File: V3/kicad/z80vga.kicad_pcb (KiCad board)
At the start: 2 copper layers, 135 x 100 mm, 53 parts, among them J2120 USB_B, J2122 Conn_01x02_Male, J2230 Micro_SD_Card_Det, SW2110 SW_Push, U1 74HCT273, U2100 Z8-L180-S180-180-PQFP-80, U2101 GAL16V8, U2102 14.7456 MHz, U2110 LM555xM, U2120 MCP2221AxP, U2230 74LS07, U2231 LP2985-3.3, U3000 SST39SF040, U3001 AS6C4008-55PCN

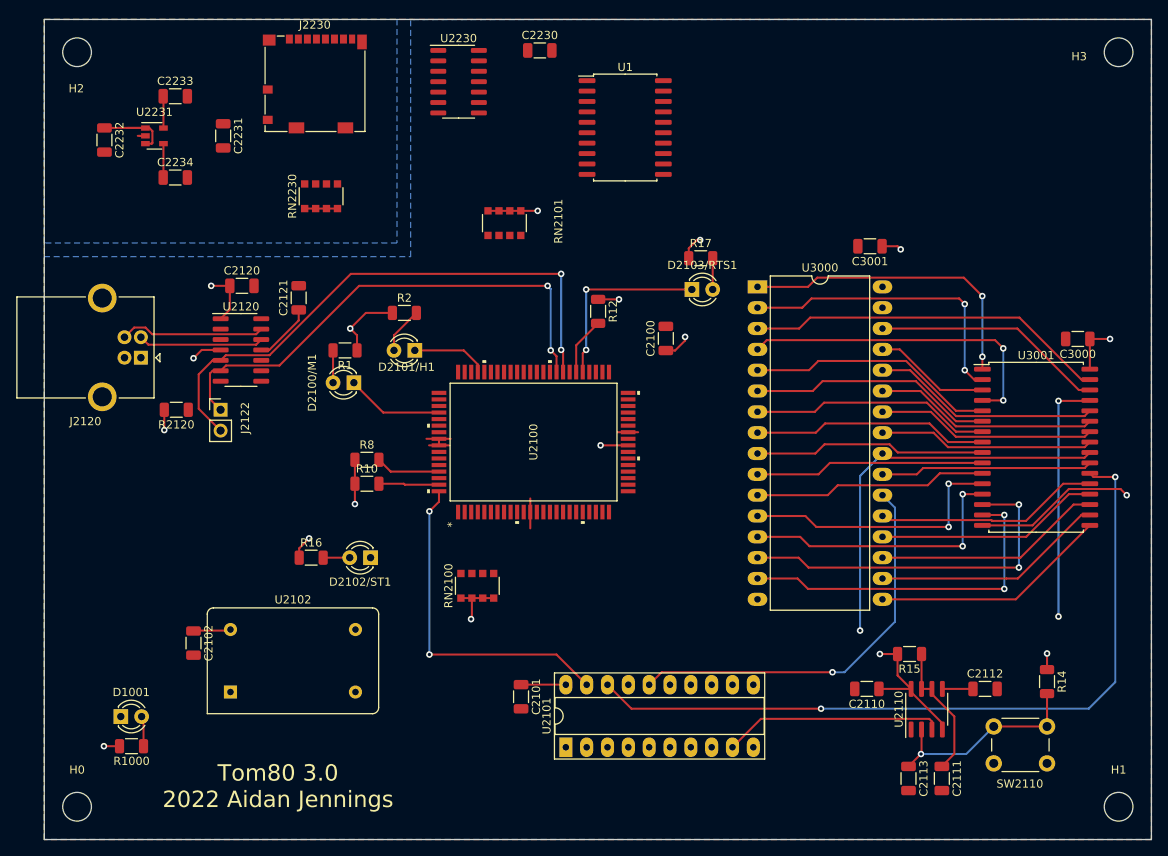
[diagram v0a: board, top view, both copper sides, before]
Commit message: 3.1 fix sheet hierarchy (#13)
* Fixed Schematic Heirarchy issue

* some footprints re-added to board

* Add footprints added

* Minor changes
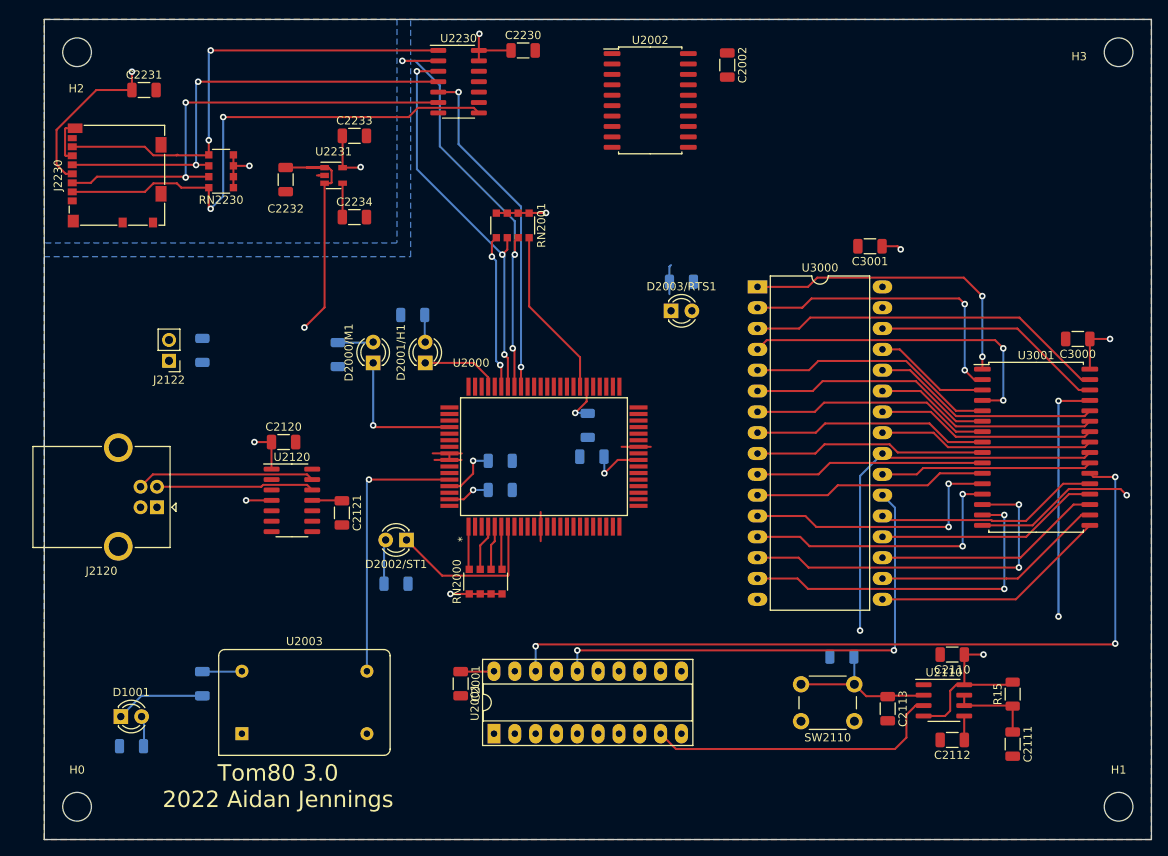
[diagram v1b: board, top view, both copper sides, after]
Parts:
- removed C2100, C2101, C2102: 22pf, Capacitor_SMD:C_1206_3216Metric
- removed D2100/M1, D2101/H1, D2102/ST1, D2103/RTS1: LED, LED_THT:LED_D3.0mm
- removed R1, R10, R12, R14, R16, R17, R2, R8: R, Resistor_SMD:R_1206_3216Metric
- removed RN2100, RN2101: 4 x 10K, Resistor_SMD:R_Array_Convex_4x1206
- removed U1: 74HCT273, Package_SO:SOIC-20W_7.5x12.8mm_P1.27mm
- removed U2100: Z8-L180-S180-180-PQFP-80, UL_Z180:Z8018008FSG
- removed U2101: GAL16V8, Package_DIP:DIP-20_W7.62mm_Socket_LongPads
- removed U2102: 14.7456 MHz, Oscillator:Oscillator_DIP-14
- added C2000: 22pf, Capacitor_SMD:C_1206_3216Metric, B.Cu at (96.8, 83.3)
- added C2001: 22pf, Capacitor_SMD:C_1206_3216Metric, F.Cu at (80.8, 111.0)
- added C2002: 22pf, Capacitor_SMD:C_1206_3216Metric, F.Cu at (113.3, 35.6)
- added C2003: 22pf, Capacitor_SMD:C_1206_3216Metric, B.Cu at (49.3, 111.0)
- added D2000/M1: LED, LED_THT:LED_D3.0mm, F.Cu at (70.1, 71.9)
- added D2001/H1: LED, LED_THT:LED_D3.0mm, F.Cu at (76.5, 71.9)
- added D2002/ST1: LED, LED_THT:LED_D3.0mm, F.Cu at (74.2, 93.5)
- added D2003/RTS1: LED, LED_THT:LED_D3.0mm, F.Cu at (106.4, 65.5)
- added R2000: R, Resistor_SMD:R_1206_3216Metric, B.Cu at (65.8, 70.9)
- added R2001: R, Resistor_SMD:R_1206_3216Metric, B.Cu at (74.9, 66.0)
- added R2002: R, Resistor_SMD:R_1206_3216Metric, B.Cu at (72.9, 98.8)
- added R2003: R, Resistor_SMD:R_1206_3216Metric, B.Cu at (107.7, 62.0)
- added R2004: R, Resistor_SMD:R_1206_3216Metric, B.Cu at (85.6, 83.8)
- added R2005: R, Resistor_SMD:R_1206_3216Metric, B.Cu at (85.6, 87.4)
- added R2006: R, Resistor_SMD:R_1206_3216Metric, B.Cu at (96.3, 79.5)
- added R2110: 1M, Resistor_SMD:R_1206_3216Metric, B.Cu at (127.3, 107.7)
- added RN2000: 4 x 10K, Resistor_SMD:R_Array_Convex_4x1206, F.Cu at (83.8, 98.6)
- added RN2001: 4 x 10K, Resistor_SMD:R_Array_Convex_4x1206, F.Cu at (87.1, 55.1)
- added U2000: Z8-L180-S180-180-PQFP-80, UL_Z180:Z8018008FSG, F.Cu at (90.9, 83.3)
- added U2001: GAL16V8, Package_DIP:DIP-20_W7.62mm_Socket_LongPads, F.Cu at (84.8, 117.1)
- added U2002: 74HCT273, Package_SO:SOIC-20W_7.5x12.8mm_P1.27mm, F.Cu at (103.9, 39.9)
- added U2003: 14.7456 MHz, Oscillator:Oscillator_DIP-14, F.Cu at (54.1, 117.1)
- R1000, R2120: moved to B.Cu
- R15: value R -> 2111
- moved C2121 26.7 mm to (66.3, 90.2), turned to 270 degrees
- moved J2230 26.6 mm to (38.9, 49.0), turned to 90 degrees
- moved SW2110 24.1 mm to (128.8, 115.6)
- moved C2232 22.6 mm to (59.4, 49.5)
- moved U2231 22.4 mm to (65.3, 49.0)
- moved C2233 22.4 mm to (67.8, 44.2)
- moved C2234 22.4 mm to (67.8, 54.1)
- moved C2120 19.7 mm to (59.2, 81.5)
- moved U2120 19.4 mm to (60.2, 88.6)
- moved J2120 18.3 mm to (43.7, 89.5)
- moved R15 13.5 mm to (148.1, 112.3), turned to 90 degrees
- moved RN2230 12.6 mm to (51.6, 48.5), turned to 180 degrees
- moved C2110 11.2 mm to (140.7, 107.4)
- moved C2231 11.2 mm to (42.2, 38.6), turned to 0 degrees
- moved C2111 9.60 mm to (148.1, 118.4)
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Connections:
- net /2000_Z80/2100_ALTCPU/2230_SD_Card/SD_CS renamed /2000_CPU/2230_SD_Card/SD_CS
- net /2000_Z80/2100_ALTCPU/2230_SD_Card/SD_MISO renamed /2000_CPU/2230_SD_Card/SD_MISO
- net /2000_Z80/2100_ALTCPU/RX renamed /2000_CPU/RX
- net /2000_Z80/2100_ALTCPU/TX renamed /2000_CPU/TX
- net /2000_Z80/RD renamed /2000_CPU/RD
- net /3000_Memory/A0 renamed /2000_CPU/A0
- net /3000_Memory/A1 renamed /2000_CPU/A1
- net /3000_Memory/A10 renamed /2000_CPU/A10
- net /3000_Memory/A11 renamed /2000_CPU/A11
- net /3000_Memory/A12 renamed /2000_CPU/A12
- net /3000_Memory/A13 renamed /2000_CPU/A13
- net /3000_Memory/A14 renamed /2000_CPU/A14
- net /3000_Memory/A15 renamed /2000_CPU/A15
- net /3000_Memory/A16 renamed /2000_CPU/A16
- net /3000_Memory/A17 renamed /2000_CPU/A17
- net /3000_Memory/A18 renamed /2000_CPU/A18
- net /3000_Memory/A2 renamed /2000_CPU/A2
- net /3000_Memory/A3 renamed /2000_CPU/A3
- net /3000_Memory/A4 renamed /2000_CPU/A4
- net /3000_Memory/A5 renamed /2000_CPU/A5
- net /3000_Memory/A6 renamed /2000_CPU/A6
- net /3000_Memory/A7 renamed /2000_CPU/A7
- net /3000_Memory/A8 renamed /2000_CPU/A8
- net /3000_Memory/A9 renamed /2000_CPU/A9
- net /3000_Memory/D0 renamed /2000_CPU/D0
- net /3000_Memory/D1 renamed /2000_CPU/D1
- net /3000_Memory/D2 renamed /2000_CPU/D2
- net /3000_Memory/D3 renamed /2000_CPU/D3
- net /3000_Memory/D4 renamed /2000_CPU/D4
- net /3000_Memory/D5 renamed /2000_CPU/D5
- net /3000_Memory/D6 renamed /2000_CPU/D6
- net /3000_Memory/D7 renamed /2000_CPU/D7
- J2230 pad 3: /2000_Z80/2100_ALTCPU/2230_SD_Card/SD_MOSI -> /2000_CPU/2230_SD_Card/SD_MOSI
- J2230 pad 5: /2000_Z80/2100_ALTCPU/2230_SD_Card/SD_SCK -> /2000_CPU/2230_SD_Card/SD_SCK
- RN2230 pad 6: /2000_Z80/2100_ALTCPU/2230_SD_Card/SD_MOSI -> /2000_CPU/2230_SD_Card/SD_SCK
- RN2230 pad 7: /2000_Z80/2100_ALTCPU/2230_SD_Card/SD_SCK -> /2000_CPU/2230_SD_Card/SD_MOSI
- U2110 pad 3: /2000_Z80/2100_ALTCPU/2110_Reset/Reset -> /2000_CPU/2110_Reset/Reset
- U2230 pad 2: /2000_Z80/2100_ALTCPU/RXS -> /2000_CPU/RXS
- U2230 pad 3: /2000_Z80/2100_ALTCPU/CKS -> /2000_CPU/CKS
- U2230 pad 4: /2000_Z80/2100_ALTCPU/2230_SD_Card/SD_SCK -> /2000_CPU/2230_SD_Card/SD_SCK
- U2230 pad 5: /2000_Z80/2100_ALTCPU/TXS -> /2000_CPU/TXS
- U2230 pad 6: /2000_Z80/2100_ALTCPU/2230_SD_Card/SD_MOSI -> /2000_CPU/2230_SD_Card/SD_MOSI
- U2230 pad 9: /2000_Z80/2100_ALTCPU/CS0 -> /2000_CPU/CS0
- U3000 pad 22: /2000_Z80/ROM_CS -> /2000_CPU/ROM_CS
- U3001 pad 22: /2000_Z80/RAM_CS -> /2000_CPU/RAM_CS
- U3001 pad 29: /2000_Z80/WR -> /2000_CPU/WR
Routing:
- net /2000_CPU/RAM_CS: track 0.00 -> 97.5 mm, vias 0 -> 3
- net /2000_Z80/RAM_CS: track 92.8 -> 0.00 mm, vias 2 -> 0
- net /2000_CPU/TX: track 69.3 -> 0.00 mm, vias 2 -> 0
- net /2000_CPU/2230_SD_Card/SD_CS: track 0.00 -> 63.7 mm, vias 0 -> 2
- net /2000_CPU/RX: track 61.5 -> 0.00 mm, vias 2 -> 0
- net /2000_CPU/ROM_CS: track 0.00 -> 60.8 mm, vias 0 -> 2
- net /2000_CPU/2230_SD_Card/SD_MISO: track 0.00 -> 57.8 mm, vias 0 -> 2
- net /2000_CPU/2230_SD_Card/SD_MOSI: track 0.00 -> 57.0 mm, vias 0 -> 2
- net /2000_CPU/2230_SD_Card/SD_SCK: track 0.00 -> 56.5 mm, vias 0 -> 2
- net /2000_CPU/RXS: track 0.00 -> 53.1 mm, vias 0 -> 3
- net /2000_Z80/ROM_CS: track 49.2 -> 0.00 mm, vias 1 -> 0
- net /2000_CPU/CKS: track 0.00 -> 48.0 mm, vias 0 -> 3
- net /2000_CPU/TXS: track 0.00 -> 41.5 mm, vias 0 -> 2
- net /2000_Z80/2100_ALTCPU/C_RST: track 41.1 -> 0.00 mm, vias 2 -> 0
- net /2000_CPU/2110_Reset/Reset: track 0.00 -> 36.7 mm
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
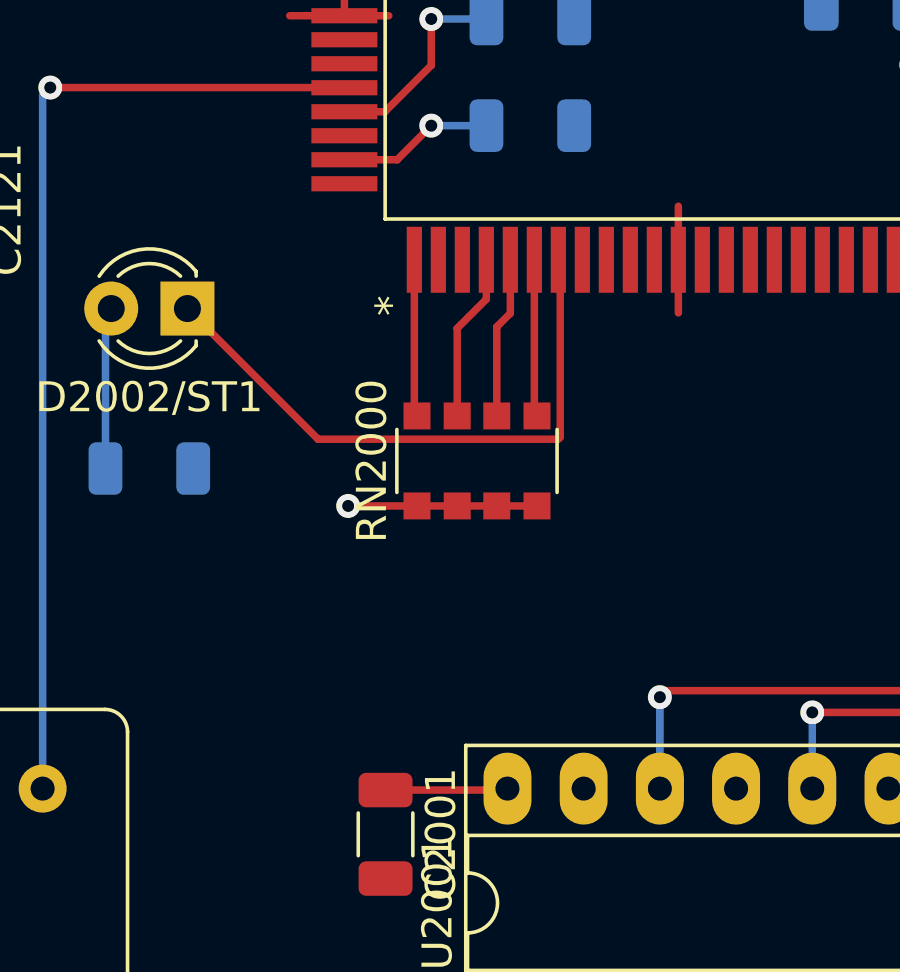
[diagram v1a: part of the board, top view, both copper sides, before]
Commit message: 3.1 redraw cpu courtyard (#14)
* moved all crtyd lines to same place in file

* Duplicate lines were causing issues
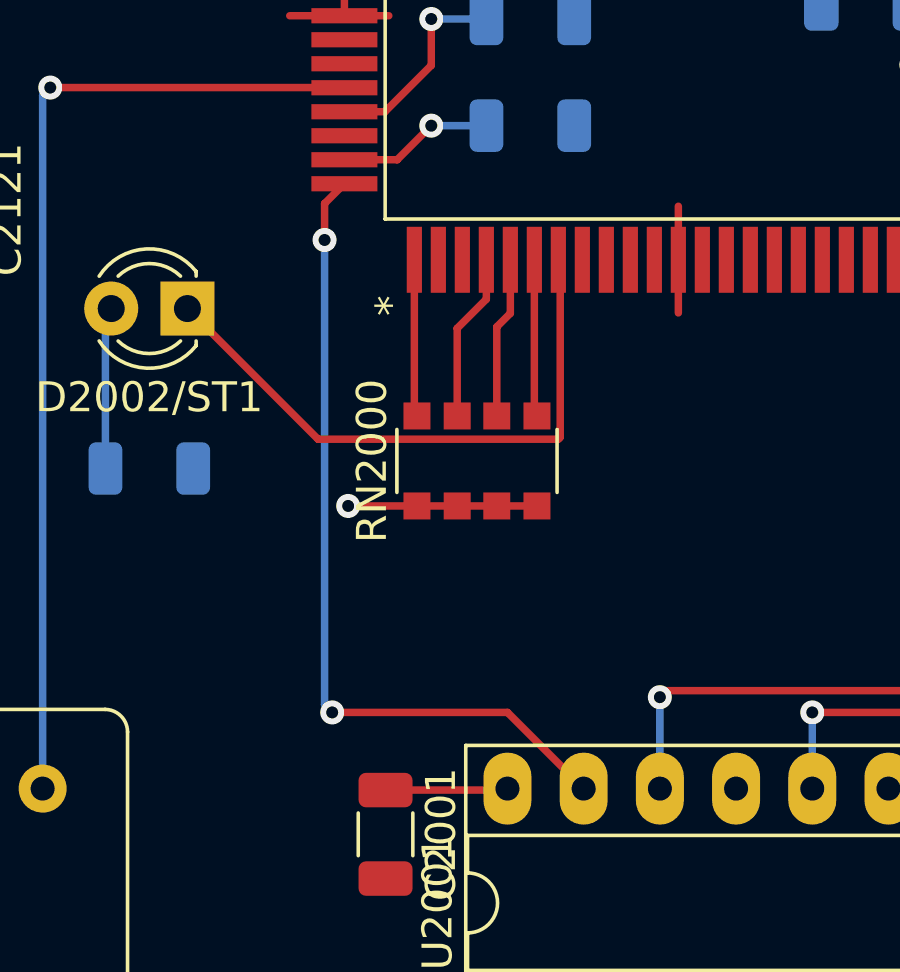
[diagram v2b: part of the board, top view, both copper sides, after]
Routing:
- net /2000_CPU/C_RST: track 0.00 -> 27.4 mm, vias 0 -> 2

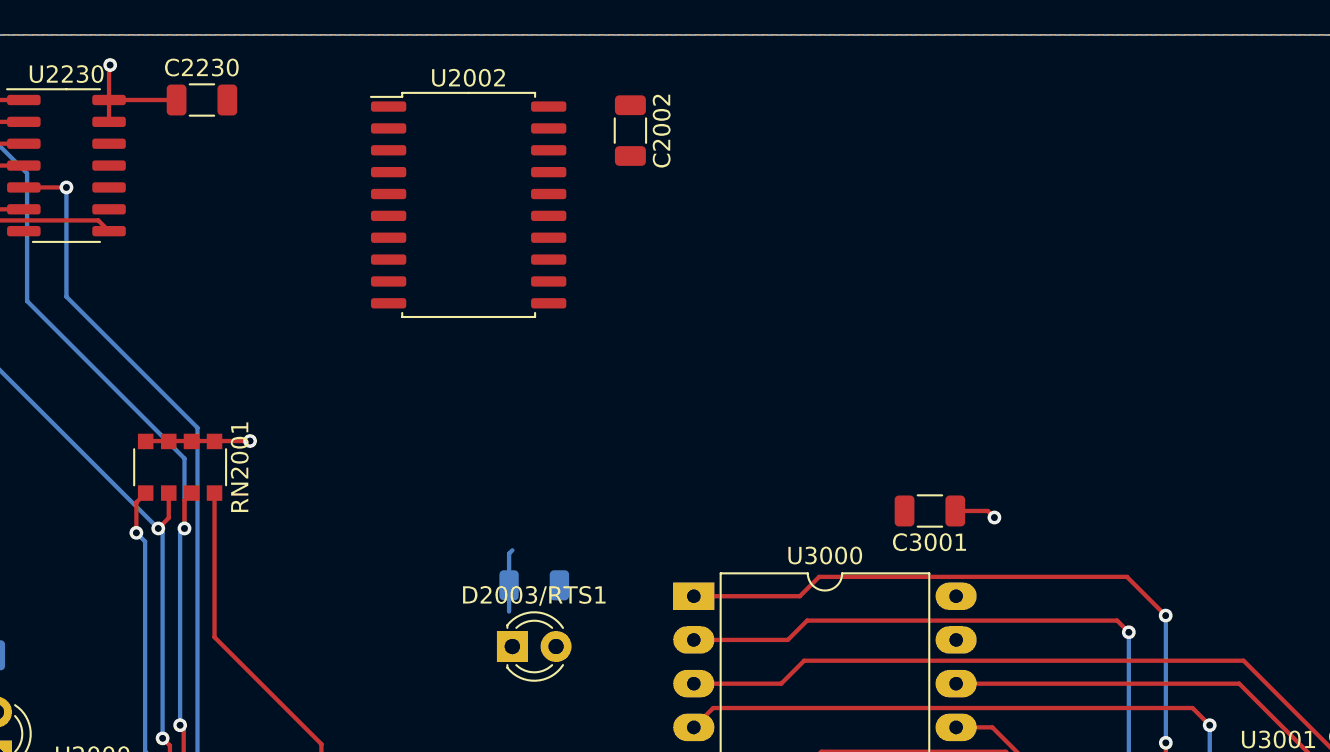
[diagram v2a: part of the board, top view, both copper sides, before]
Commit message: Added pin header for SPI lines
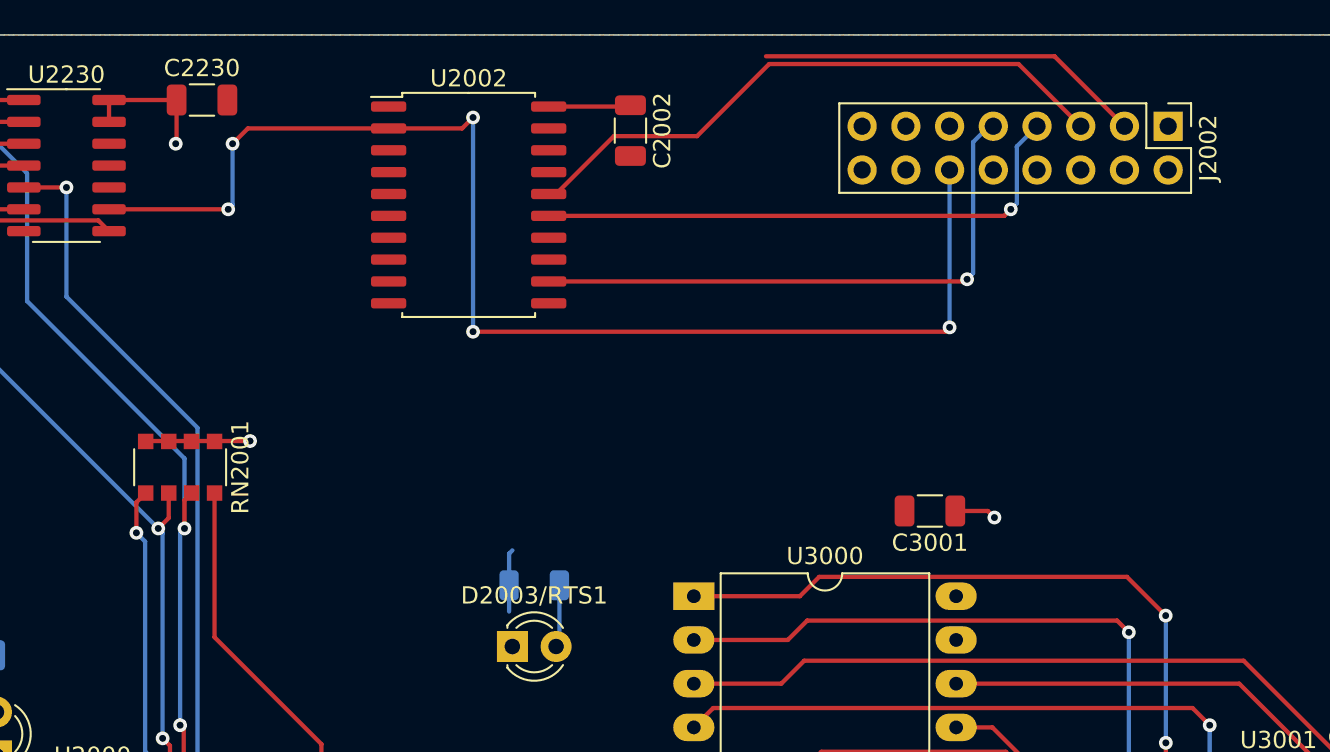
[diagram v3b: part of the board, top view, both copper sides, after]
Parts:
- added J2002: Conn_02x08_Odd_Even, Connector_PinHeader_2.54mm:PinHeader_2x08_P2.54mm_Vertical, F.Cu at (144.5, 35.3)
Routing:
- net /2000_CPU/CS0: track 0.00 -> 74.8 mm, vias 0 -> 5
- net /2000_CPU/CS6: track 0.00 -> 35.5 mm
- net /2000_CPU/CS4: track 0.00 -> 34.0 mm, vias 0 -> 1
- net /2000_CPU/CS5: track 0.00 -> 32.5 mm, vias 0 -> 1
- net /2000_CPU/CS7: track 0.00 -> 22.5 mm
- net +5V: track 105.2 -> 110.5 mm
- net Net-(D2003/RTS1-Pad2): track 0.00 -> 3.64 mm
